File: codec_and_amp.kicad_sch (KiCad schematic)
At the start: 32 parts, among them J1 Conn_01x08, J2 Conn_01x06, U1 TLV320AIC3206IRSBR, U4 FSA2275UMX, U6 MIC5504-1.8YM5, U7 TPD4E02B04DQAR, U8 TPD4E02B04DQAR

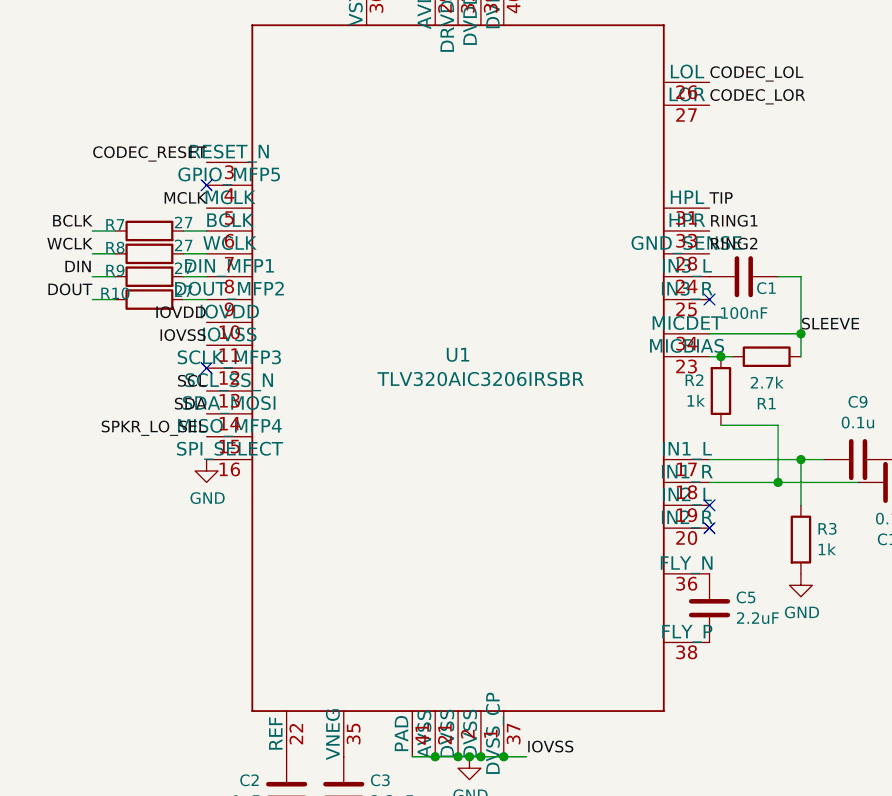
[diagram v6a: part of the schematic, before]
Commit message: Add connector for side buttons; wire up to the last remaining GPIO pins, and wire volume up/down to MFP3/MFP5 pins on the audio codec.
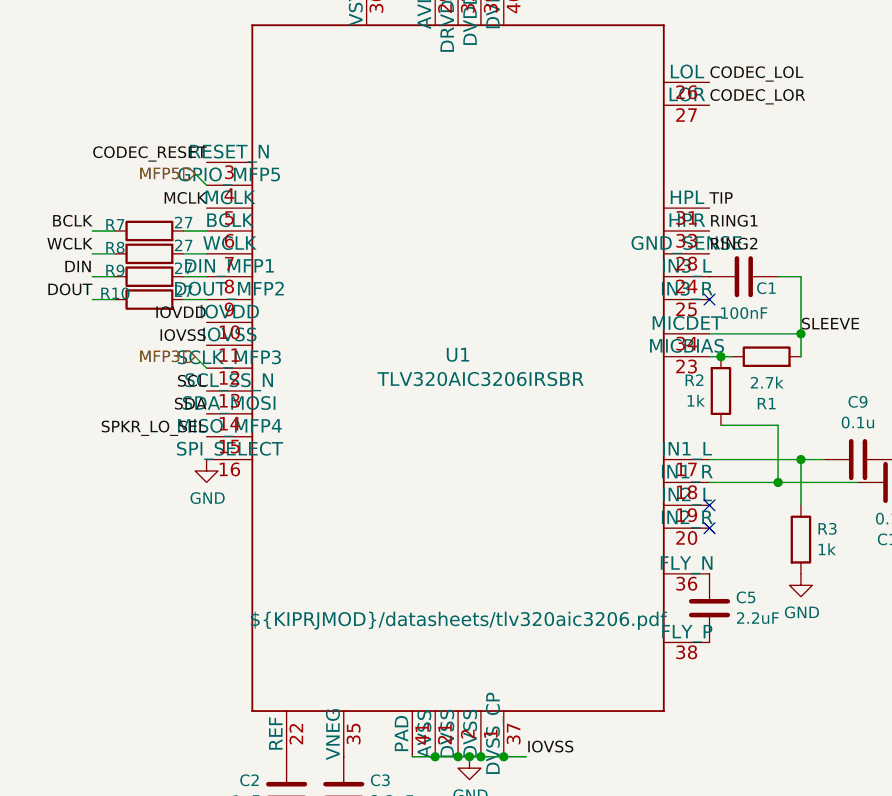
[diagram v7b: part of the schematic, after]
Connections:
- net MFP3: now reaches U1.12 (SCLK_MFP3)
- net MFP5: now reaches U1.4 (GPIO_MFP5)
- no-connect marks 5 -> 3
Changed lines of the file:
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@@
   (junction (at 293.37 82.55) (diameter 1.016) (color 0 0 0 0))
   (junction (at 295.91 85.09) (diameter 1.016) (color 0 0 0 0))
-  (no_connect (at 29.21 104.14))
-  (no_connect (at 29.21 124.46))
   (no_connect (at 85.09 116.84))
   (no_connect (at 85.09 139.7))
@@
     (stroke (width 0) (type solid) (color 0 0 0 0))
   )
+  (wire (pts (xy 27.94 102.87) (xy 29.21 104.14))
+    (stroke (width 0) (type solid) (color 0 0 0 0))
+  )
+  (wire (pts (xy 27.94 123.19) (xy 29.21 124.46))
+    (stroke (width 0) (type solid) (color 0 0 0 0))
+  )
   (wire (pts (xy 30.48 22.86) (xy 46.99 22.86))
     (stroke (width 0) (type solid) (color 0 0 0 0))
@@
   (label "RING1" (at 308.61 85.09 180)
     (effects (font (size 1.27 1.27)) (justify right bottom))
+  )
+  (hierarchical_label "MFP5" (shape input) (at 27.94 102.87 180)
+    (effects (font (size 1.27 1.27)) (justify right))
+  )
+  (hierarchical_label "MFP3" (shape input) (at 27.94 123.19 180)
+    (effects (font (size 1.27 1.27)) (justify right))
   )
   (hierarchical_label "VSYS" (shape input) (at 29.21 43.18 0)
@@
       (effects (font (size 1.524 1.524)) hide)
     )
-    (property "Datasheet" "" (id 3) (at 57.15 152.4 0)
+    (property "Datasheet" "${KIPRJMOD}/datasheets/tlv320aic3206.pdf" (id 3) (at 57.15 152.4 0)
       (effects (font (size 1.524 1.524)))
     )

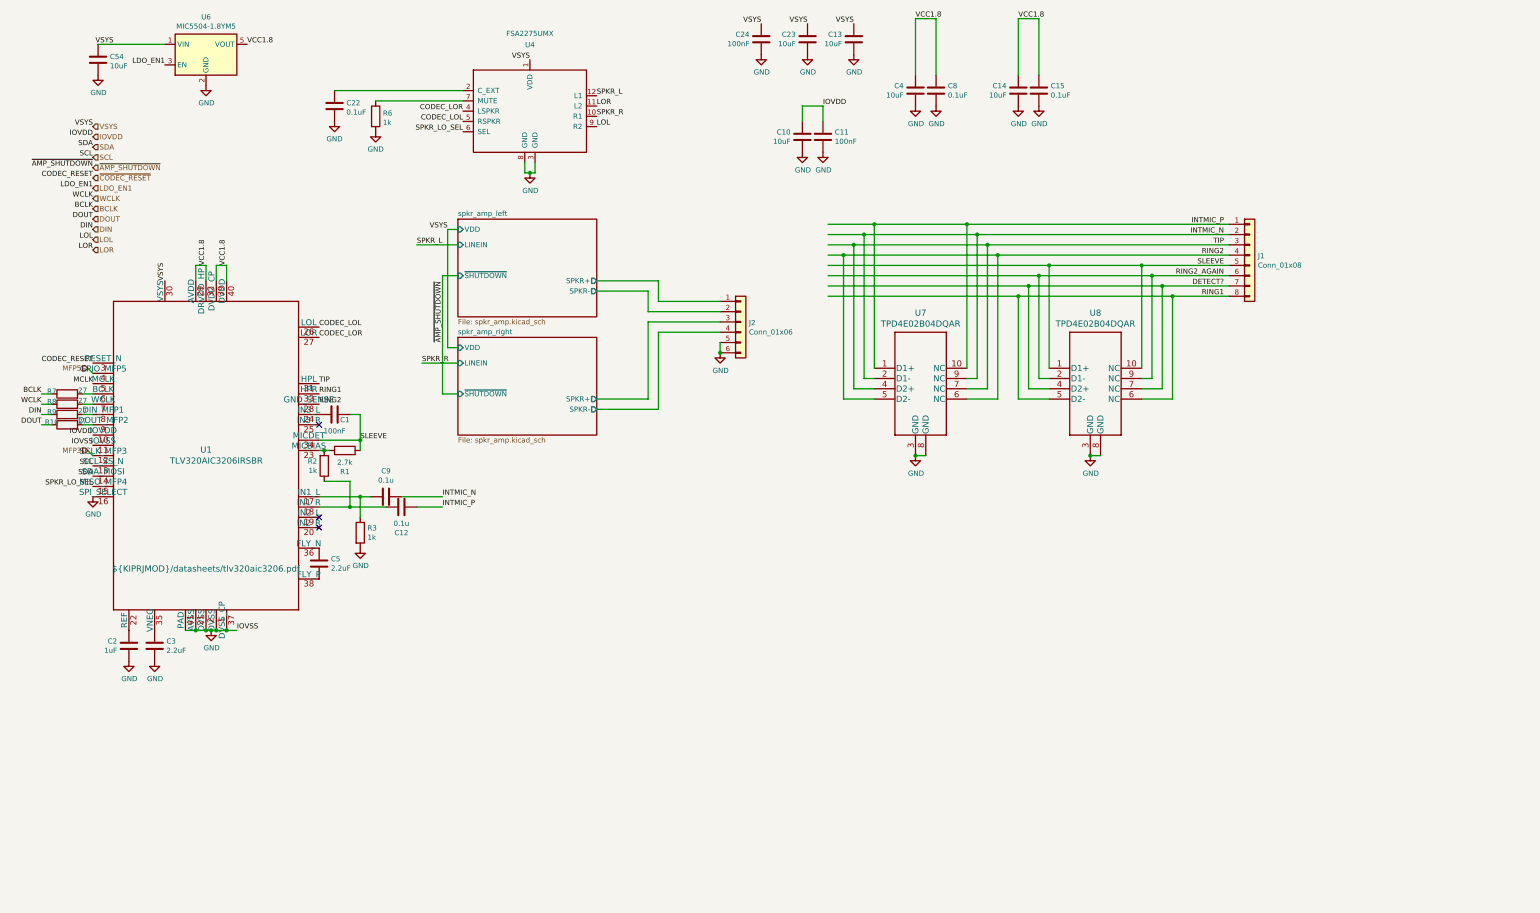
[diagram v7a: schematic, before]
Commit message: Route CM4 board with differential connector on the right.
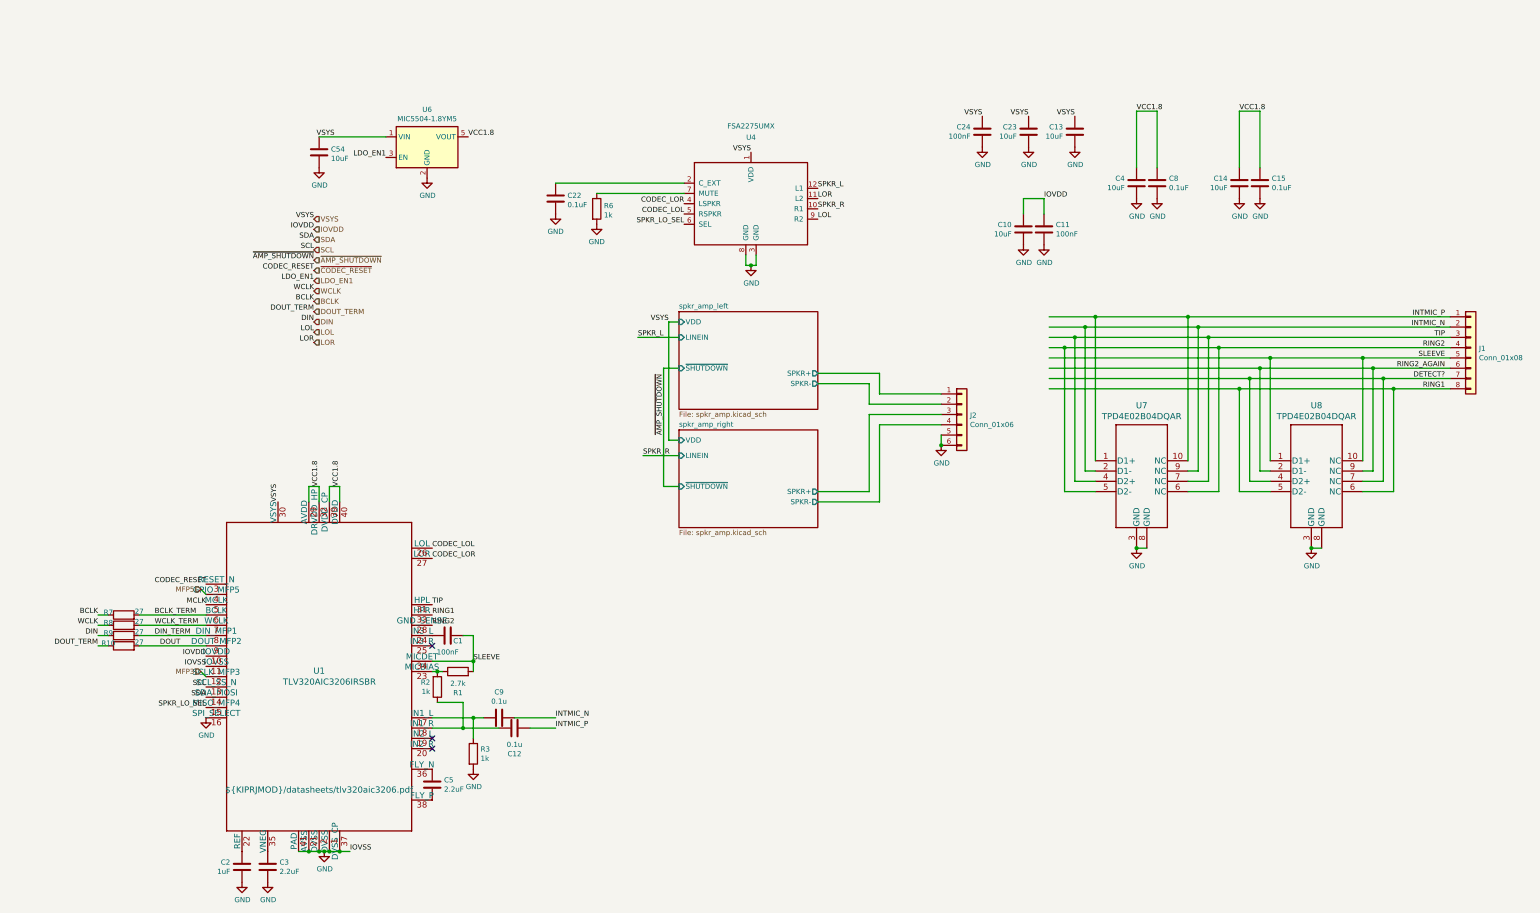
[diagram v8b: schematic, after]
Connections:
- net DOUT: now also R10.2, U1.9 (DOUT_MFP2); no longer R10.1
- net BCLK_TERM: now reaches R7.2, U1.6 (BCLK)
- net WCLK_TERM: now reaches R8.2, U1.7 (WCLK)
- net DIN_TERM: now reaches R9.2, U1.8 (DIN_MFP1)
- net ~CODEC_RESET renamed ~{CODEC_RESET}
- new net DOUT_TERM: R10.1
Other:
- sheet spkr_amp_left ports: added ~{SHUTDOWN}; removed ~SHUTDOWN
- sheet spkr_amp_right ports: added ~{SHUTDOWN}; removed ~SHUTDOWN
- moved on the sheet: C1, C10, C11, C12, C13, C14, C15, C2, C22, C23, C24, C3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
